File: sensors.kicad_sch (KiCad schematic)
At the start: 7 parts, among them U3 LSM303AGRTR, U4 BMI088

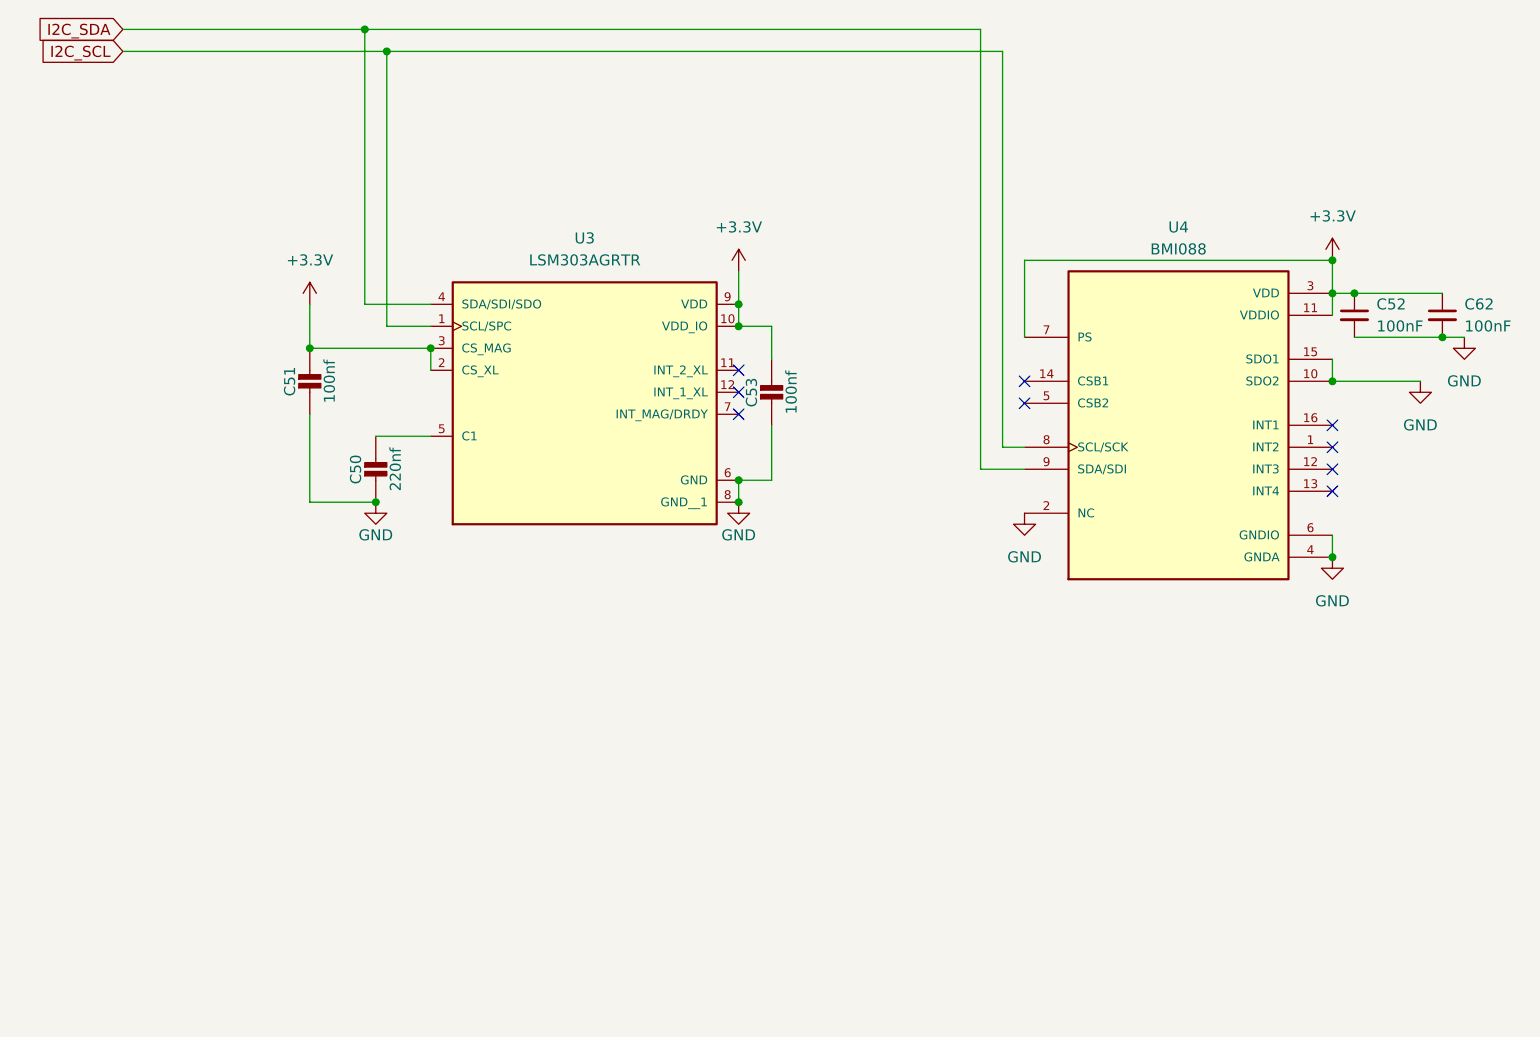
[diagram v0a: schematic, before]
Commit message: changed mounting holes
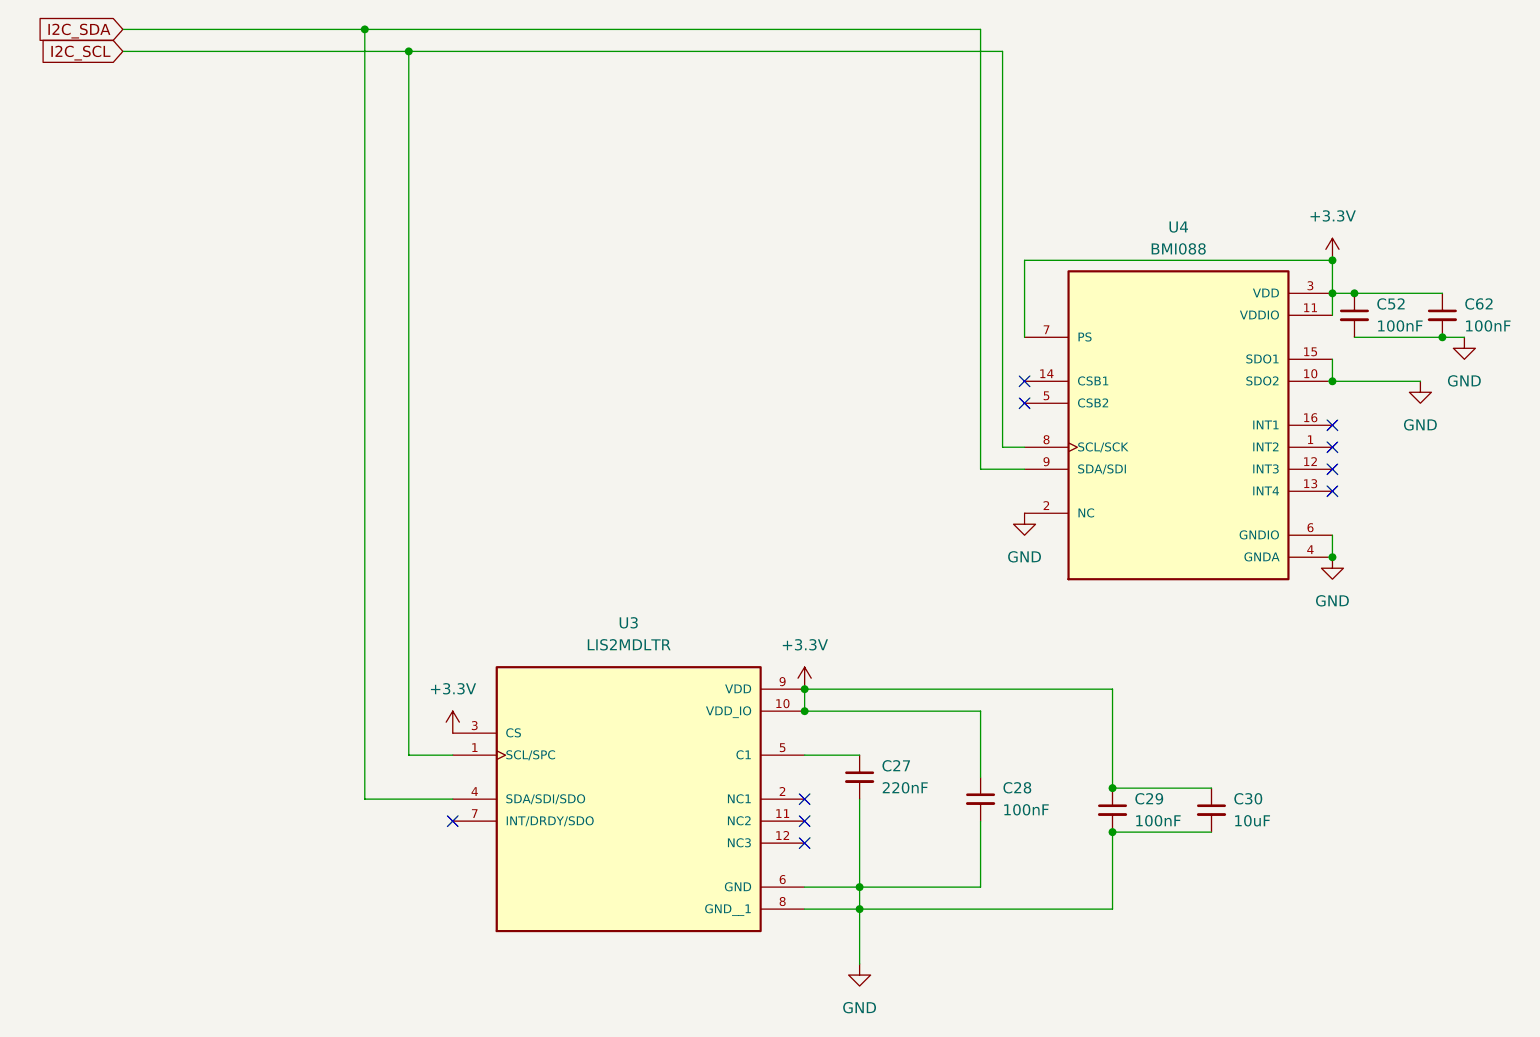
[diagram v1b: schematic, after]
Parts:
- removed C50: 220nf, Capacitor_SMD:C_0402_1005Metric, symbol Adafruit ItsyBitsy RP2040-eagle-import:CAP_CERAMIC_0402NO
- removed C51, C53: 100nf, Capacitor_SMD:C_0402_1005Metric, symbol Adafruit ItsyBitsy RP2040-eagle-import:CAP_CERAMIC_0402NO
- removed U3: LSM303AGRTR, footprints:LGA12R50P_200X200X100, symbol LSM303AGRTR:LSM303AGRTR
- added C27: 220nF, Capacitor_SMD:C_0402_1005Metric, symbol Device:C_Small
- added C28, C29: 100nF, Capacitor_SMD:C_0402_1005Metric, symbol Device:C_Small
- added C30: 10uF, Capacitor_SMD:C_0402_1005Metric, symbol Device:C_Small
- added U3: LIS2MDLTR, footprints:PQFN50P200X200X70-12N, symbol LIS2MDLTR:LIS2MDLTR
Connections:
- net +3.3V: now also C28.1, C29.1, C30.1, U3.10 (VDD_IO), U3.3 (CS), U3.9 (VDD)
- net GND: now also C27.2, C28.2, C29.2, C30.2, U3.6 (GND), U3.8 (GND__1)
- net I2C_SCL: now also U3.1 (SCL/SPC)
- net I2C_SDA: now also U3.4 (SDA/SDI/SDO)
- new net: C27.1, U3.5 (C1)
- no-connect marks 9 -> 10
